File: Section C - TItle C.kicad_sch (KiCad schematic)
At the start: 1 part, among them U2 LT3042xMSE

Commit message: [Schématique test]
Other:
- moved on the sheet: U2
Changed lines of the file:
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@@
 	(symbol
 		(lib_id "Regulator_Linear:LT3042xMSE")
-		(at 203.2 68.58 0)
+		(at 228.6 72.39 0)
 		(unit 1)
 		(exclude_from_sim no)
@@
 		(fields_autoplaced yes)
 		(property "Reference" "U2"
-			(at 203.2 58.42 0)
+			(at 228.6 62.23 0)
 			(effects
 				(font
@@
 		)
 		(property "Value" "LT3042xMSE"
-			(at 203.2 60.96 0)
+			(at 228.6 64.77 0)
 			(effects
 				(font
@@
 		)
 		(property "Footprint" "Package_SO:MSOP-10-1EP_3x3mm_P0.5mm_EP2.2x3.1mm_Mask1.83x1.89mm_ThermalVias"
-			(at 203.2 60.325 0)
+			(at 228.6 64.135 0)
 			(effects
 				(font
@@
 		)
 		(property "Datasheet" "https://www.analog.com/media/en/technical-documentation/data-sheets/3042fb.pdf"
-			(at 203.2 68.58 0)
+			(at 228.6 72.39 0)
 			(effects
 				(font
@@
 		)
 		(property "Description" "200mA, Adjustable, Ultralow Noise, Ultrahigh PSRR RF Linear Regulator, MSOP-10"
-			(at 203.2 68.58 0)
+			(at 228.6 72.39 0)
 			(effects
 				(font

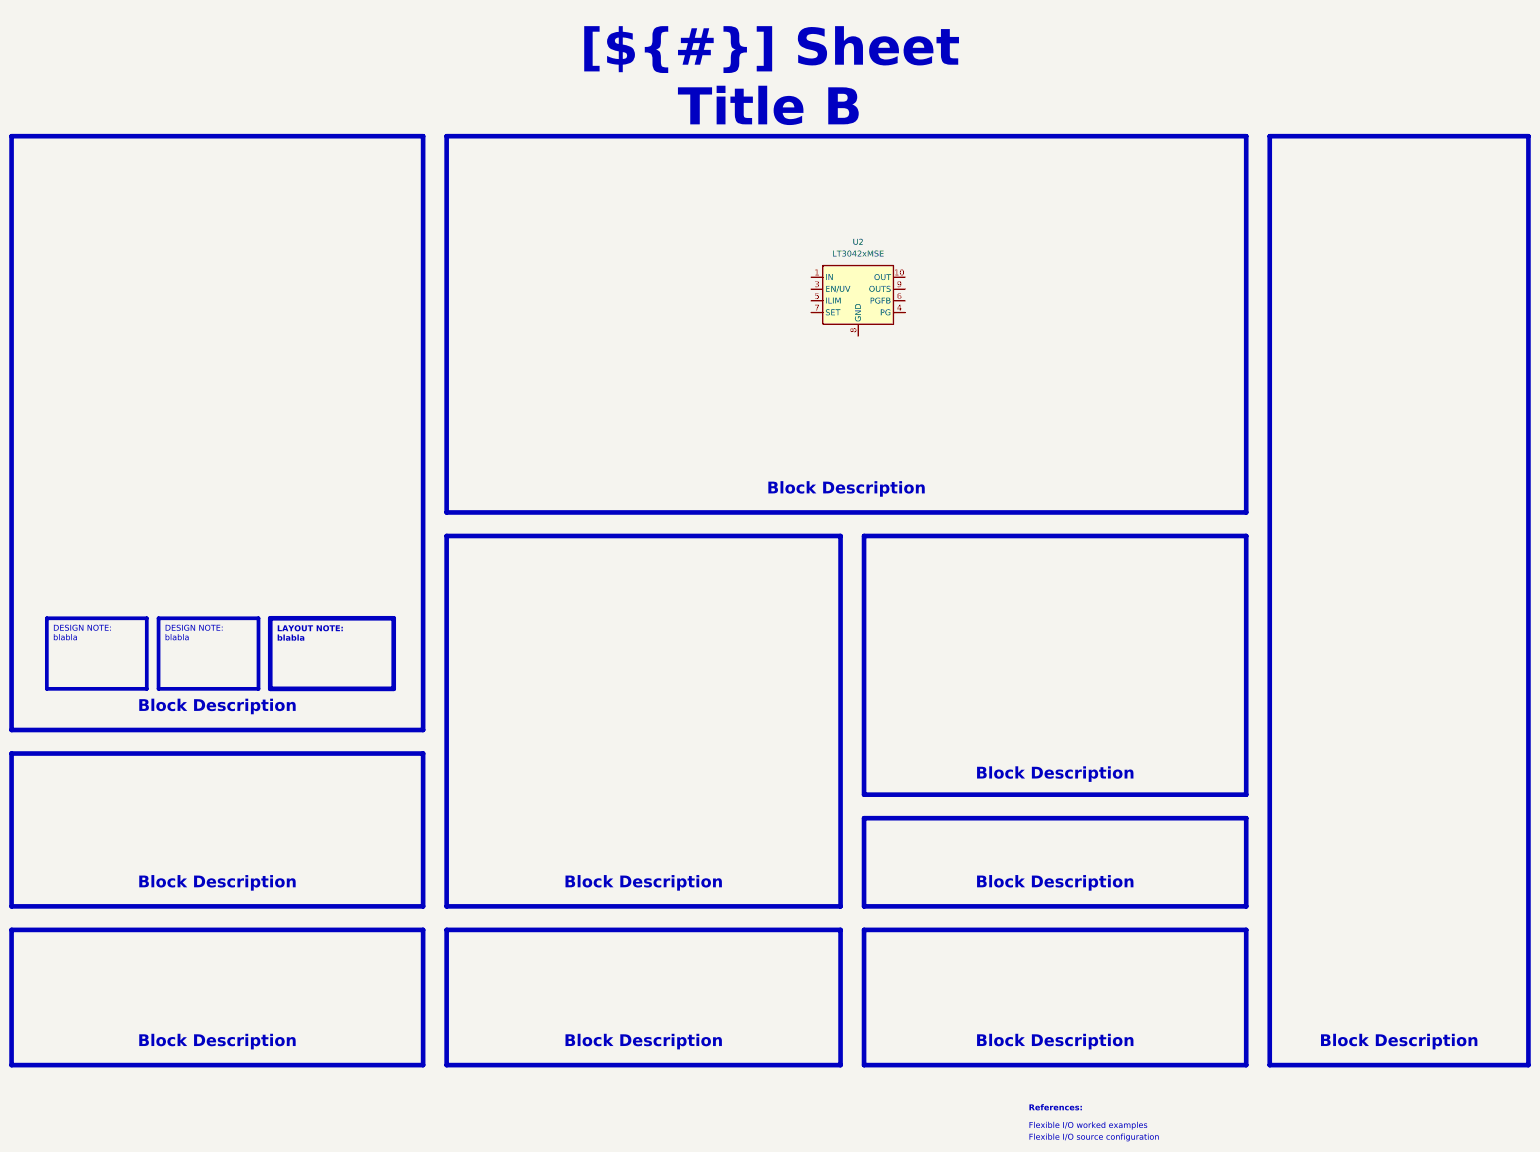
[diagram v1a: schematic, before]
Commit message: [FINISH LT3042 and ad TPS6108]
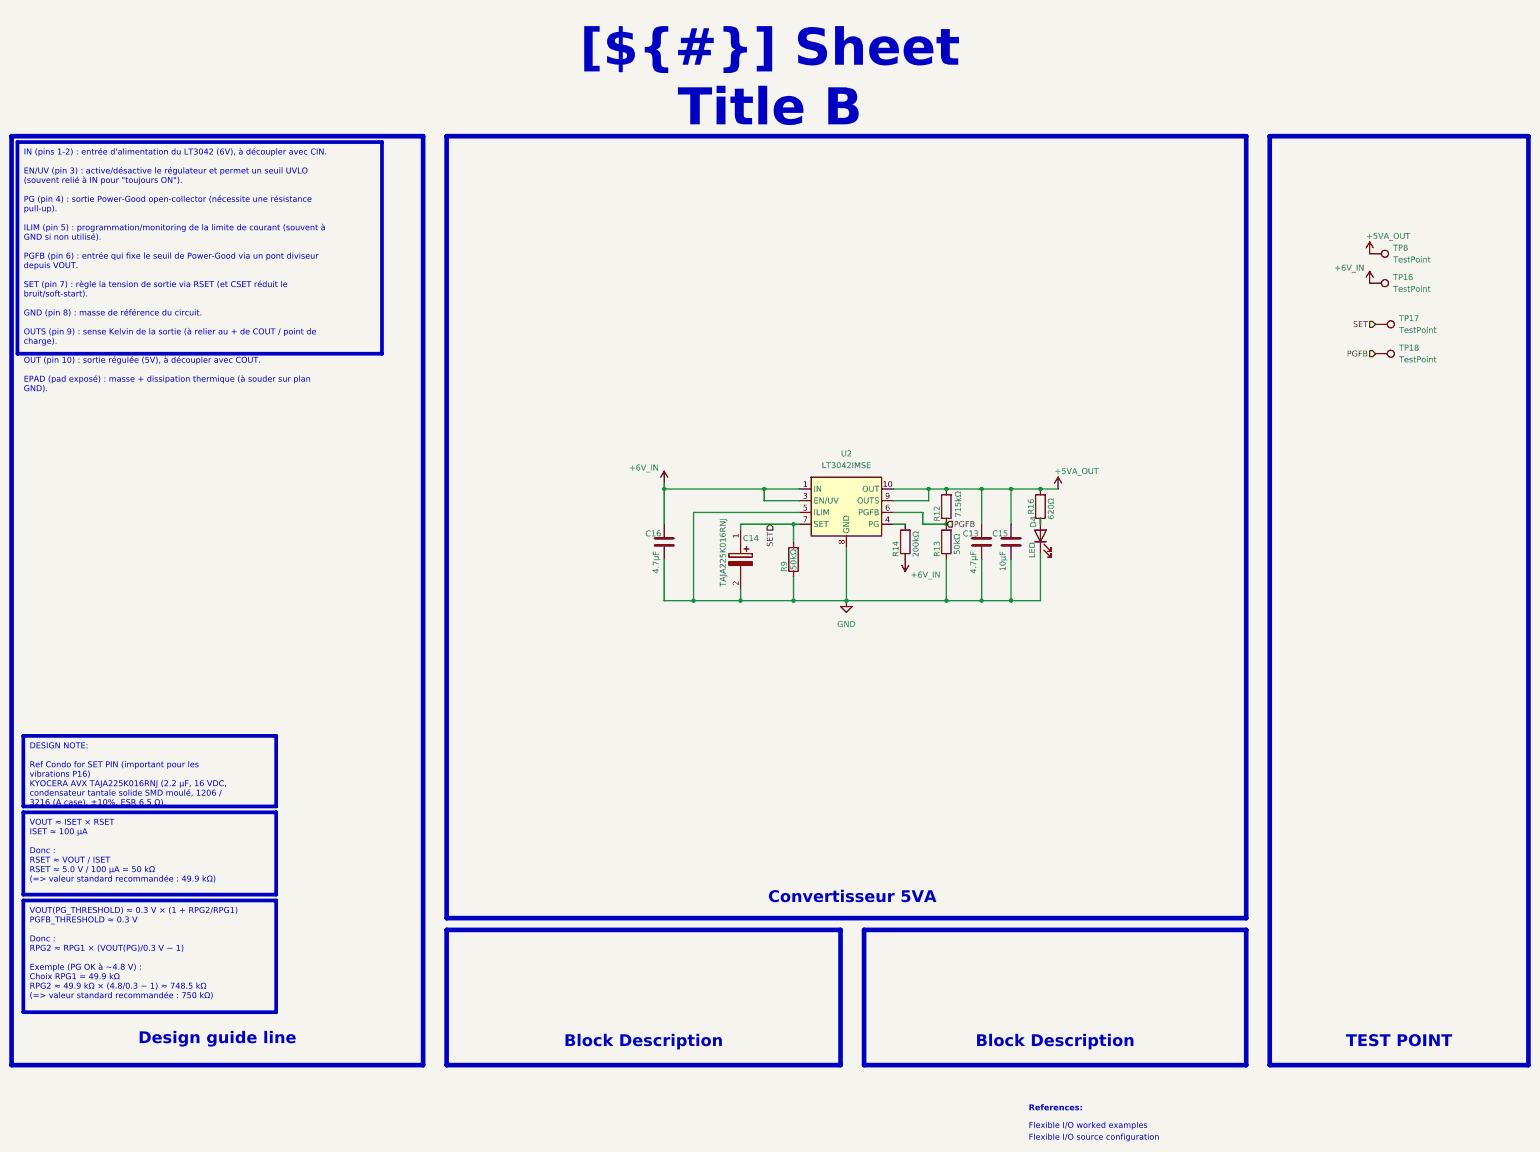
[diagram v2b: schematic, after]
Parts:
- added C13, C16: 4.7µF, Capacitor_SMD:C_0603_1608Metric, symbol Device:C
- added C14: TAJA225K016RNJ, CAPPM3216X180N, symbol TAJA225K016RNJ:TAJA225K016RNJ
- added C15: 10µF, Capacitor_SMD:C_0603_1608Metric, symbol Device:C
- added D4: LED, LED_SMD:LED_0603_1608Metric, symbol Device:LED
- added R12: 715kΩ, Resistor_SMD:R_0603_1608Metric, symbol Device:R
- added R13, R9: 50kΩ, Resistor_SMD:R_0603_1608Metric, symbol Device:R
- added R14: 200kΩ, Resistor_SMD:R_0603_1608Metric, symbol Device:R
- added R16: 620Ω, Resistor_SMD:R_0603_1608Metric, symbol Device:R
- added TP16, TP17, TP18, TP8: TestPoint, TestPoint:TestPoint_Pad_D2.0mm, symbol Connector:TestPoint
- U2: value LT3042xMSE -> LT3042IMSE
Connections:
- net +6V_IN: now reaches U2.1 (IN), U2.2 (IN)
- net +6V_IN: now also U2.3 (EN/UV), C16.1, R14.1, TP16.1
- net +5VA_OUT: now reaches U2.10 (OUT)
- net +5VA_OUT: now also U2.9 (OUTS), C13.1, C15.1, R12.2, R16.2, TP8.1
- net GND: now reaches U2.11 (GND), U2.8 (GND)
- net GND: now also U2.5 (ILIM), C13.2, C14.2 (-), C15.2, C16.2, D4.1 (K), R13.1, R9.1
- net at U2.4 (PG): now also R14.2
- net PGFB: now reaches U2.6 (PGFB)
- net PGFB: now also R12.1, R13.2, TP18.1
- net SET: now reaches U2.7 (SET)
- net SET: now also C14.1 (+), R9.2, TP17.1
- new net: D4.2 (A), R16.1
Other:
- moved on the sheet: U2

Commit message: [ADD TPS6108]
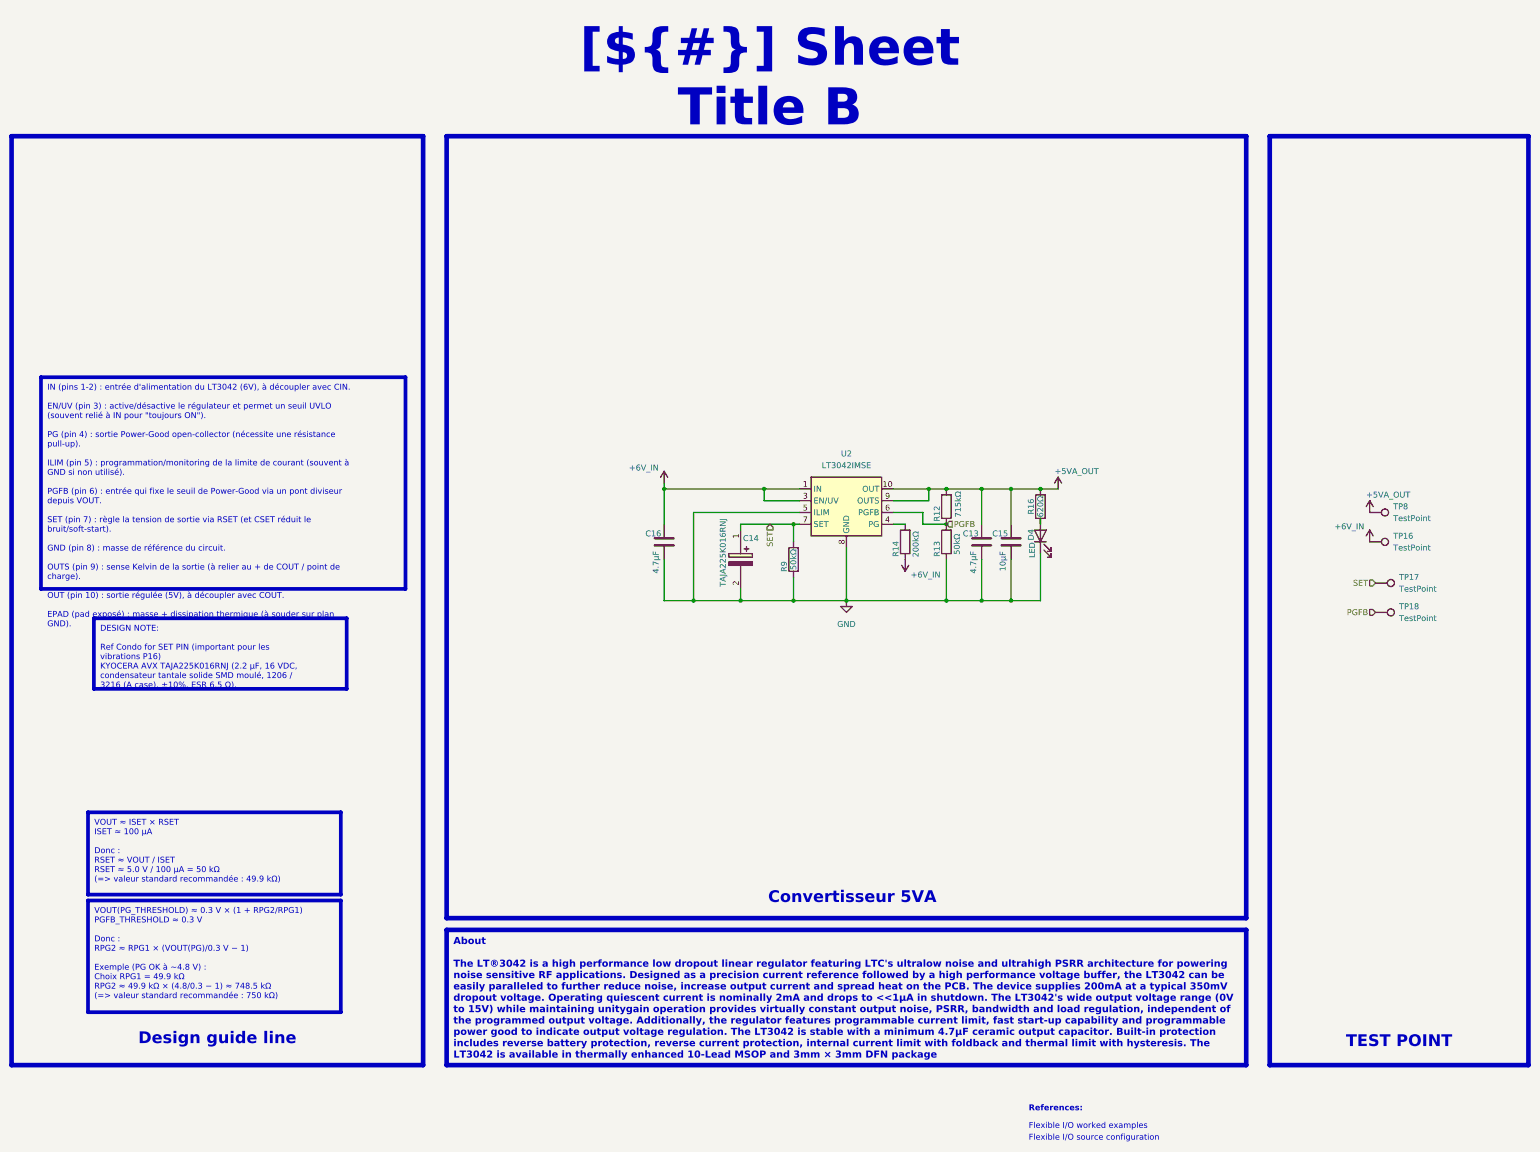
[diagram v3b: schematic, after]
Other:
- moved on the sheet: TP16, TP17, TP18, TP8

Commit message: [Finish schématique]
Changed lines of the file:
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@@
+	(wire
+		(pts
+			(xy 250.19 123.19) (xy 247.65 123.19)
+		)
+		(stroke
+			(width 0)
+			(type default)
+		)
+	)
 	(wire
 		(pts
@@
 	(wire
 		(pts
+			(xy 334.01 142.24) (xy 340.36 142.24)
+		)
+		(stroke
+			(width 0)
+			(type default)
+		)
+	)
+	(wire
+		(pts
 			(xy 243.84 118.11) (xy 243.84 115.57)
 		)
@@
 		(pts
 			(xy 226.06 128.27) (xy 226.06 139.7)
+		)
+		(stroke
+			(width 0)
+			(type default)
+		)
+	)
+	(wire
+		(pts
+			(xy 334.01 135.89) (xy 340.36 135.89)
 		)
 		(stroke
@@
 		)
 	)
-	(hierarchical_label "PGFB"
-		(shape input)
-		(at 247.65 123.19 0)
+	(label "SET"
+		(at 208.28 123.19 0)
 		(effects
 			(font
 				(size 1.27 1.27)
 			)
-			(justify left)
-		)
-	)
-	(hierarchical_label "SET"
-		(shape input)
-		(at 209.55 123.19 270)
+			(justify left bottom)
+		)
+	)
+	(label "SET"
+		(at 334.01 135.89 0)
 		(effects
 			(font
 				(size 1.27 1.27)
 			)
-			(justify right)
-		)
-	)
-	(hierarchical_label "SET"
-		(shape input)
-		(at 340.36 135.89 180)
+			(justify left bottom)
+		)
+	)
+	(label "PGFB"
+		(at 250.19 123.19 0)
 		(effects
 			(font
 				(size 1.27 1.27)
 			)
-			(justify right)
-		)
-	)
-	(hierarchical_label "PGFB"
-		(shape input)
-		(at 340.36 142.24 180)
+			(justify left bottom)
+		)
+	)
+	(label "PGFB"
+		(at 334.01 142.24 0)
 		(effects
 			(font
 				(size 1.27 1.27)
 			)
-			(justify right)
-		)
-	)
+			(justify left bottom)
+		)
+	)

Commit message: [Finish schématiq]
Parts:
- added TP23: TestPoint, TestPoint:TestPoint_Pad_D2.0mm, symbol Connector:TestPoint
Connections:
- net GND: now also TP23.1
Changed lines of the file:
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@@
 		)
 	)
-	(text_box "[${#}] ${TITLE}"
+	(text_box "[${#}] LT3042_6V_5VA"
 		(exclude_from_sim no)
 		(at 161.29 20.32 0)
-		(size 96.52 12.7)
+		(size 114.3 12.7)
 		(margins 5.9999 5.9999 5.9999 5.9999)
 		(stroke
 			(width -0.0001)
-			(type default)
+			(type solid)
 		)
 		(fill
@@
 	)
 	(symbol
+		(lib_id "power:GND")
+		(at 340.36 151.13 0)
+		(unit 1)
+		(exclude_from_sim no)
+		(in_bom yes)
+		(on_board yes)
+		(dnp no)
+		(fields_autoplaced yes)
+		(property "Reference" "#PWR037"
+			(at 340.36 157.48 0)
+			(effects
+				(font
+					(size 1.27 1.27)
+				)
+				(hide yes)
+			)
+		)
+		(property "Value" "GND"
+			(at 340.36 156.21 0)
+			(effects
+				(font
+					(size 1.27 1.27)
+				)
+			)
+		)
+		(property "Footprint" ""
+			(at 340.36 151.13 0)
+			(effects
+				(font
+					(size 1.27 1.27)
+				)
+				(hide yes)
+			)
+		)
+		(property "Datasheet" ""
+			(at 340.36 151.13 0)
+			(effects
+				(font
+					(size 1.27 1.27)
+				)
+				(hide yes)
+			)
+		)
+		(property "Description" "Power symbol creates a global label with name \"GND\" , ground"
+			(at 340.36 151.13 0)
+			(effects
+				(font
+					(size 1.27 1.27)
+				)
+				(hide yes)
+			)
+		)
+		(pin "1"
+		)
+		(instances
+			(project "Cellule_de_force_V2"
+				(path "/f9e05184-c88b-4a88-ae9c-ab2bdb32be7c/c5103ceb-5325-4a84-a025-9638a412984e/e744f3ce-03a6-44a6-8792-1447ef232b9a"
+					(reference "#PWR037")
+					(unit 1)
+				)
+			)
+		)
+	)
+	(symbol
 		(lib_id "power:+6V")
 		(at 339.09 127 0)
@@
 					(unit 1)
 				)
+			)
+		)
+	)
+	(symbol
+		(lib_id "Connector:TestPoint")
+		(at 340.36 151.13 270)
+		(unit 1)
+		(exclude_from_sim no)
+		(in_bom yes)
+		(on_board yes)
+		(dnp no)
+		(fields_autoplaced yes)
+		(property "Reference" "TP23"
+			(at 345.44 149.8599 90)
+			(effects
+				(font
+					(size 1.27 1.27)
+				)
+				(justify left)
+			)
+		)
+		(property "Value" "TestPoint"
+			(at 345.44 152.3999 90)
+			(effects
+				(font
+					(size 1.27 1.27)
+				)
+				(justify left)
+			)
+		)
+		(property "Footprint" "TestPoint:TestPoint_Pad_D2.0mm"
+			(at 340.36 156.21 0)
+			(effects
+				(font
+					(size 1.27 1.27)
+				)
+				(hide yes)
+			)
+		)
+		(property "Datasheet" "~"
+			(at 340.36 156.21 0)
+			(effects
+				(font
+					(size 1.27 1.27)
+				)
+				(hide yes)
+			)
+		)
+		(property "Description" "test point"
+			(at 340.36 151.13 0)
+			(effects
+				(font
+					(size 1.27 1.27)
+				)
+				(hide yes)
+			)
+		)
+		(pin "1"
+		)
+		(instances
+			(project "Cellule_de_force_V2"
+				(path "/f9e05184-c88b-4a88-ae9c-ab2bdb32be7c/c5103ceb-5325-4a84-a025-9638a412984e/e744f3ce-03a6-44a6-8792-1447ef232b9a"
+					(reference "TP23")
+					(unit 1)
+				)

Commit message: [PCB 4 layer]
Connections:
- net +5VA_OUT renamed +5VA
- net +6V_IN renamed +6V
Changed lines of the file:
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@@
 	(wire
 		(pts
+			(xy 335.28 151.13) (xy 340.36 151.13)
+		)
+		(stroke
+			(width 0)
+			(type default)
+		)
+	)
+	(wire
+		(pts
 			(xy 215.9 120.65) (xy 193.04 120.65)
 		)
@@
 		)
 		(property "Value" "715kΩ"
-			(at 250.19 118.872 90)
+			(at 247.65 119.38 90)
 			(effects
 				(font
-					(size 1.27 1.27)
+					(size 1.016 1.016)
 				)
 			)
@@
 	(symbol
 		(lib_id "power:GND")
-		(at 340.36 151.13 0)
+		(at 335.28 151.13 0)
 		(unit 1)
 		(exclude_from_sim no)
@@
 		(fields_autoplaced yes)
 		(property "Reference" "#PWR037"
-			(at 340.36 157.48 0)
+			(at 335.28 157.48 0)
 			(effects
 				(font
@@
 		)
 		(property "Value" "GND"
-			(at 340.36 156.21 0)
+			(at 335.28 156.21 0)
 			(effects
 				(font
@@
 		)
 		(property "Footprint" ""
-			(at 340.36 151.13 0)
+			(at 335.28 151.13 0)
 			(effects
 				(font
@@
 		)
 		(property "Datasheet" ""
-			(at 340.36 151.13 0)
+			(at 335.28 151.13 0)
 			(effects
 				(font
@@
 		)
 		(property "Description" "Power symbol creates a global label with name \"GND\" , ground"
-			(at 340.36 151.13 0)
+			(at 335.28 151.13 0)
 			(effects
 				(font
@@
 	(symbol
 		(lib_id "power:+6V")
-		(at 339.09 127 0)
+		(at 339.09 127 90)
 		(unit 1)
 		(exclude_from_sim no)
@@
 		(dnp no)
 		(property "Reference" "#PWR021"
-			(at 339.09 130.81 0)
+			(at 342.9 127 0)
 			(effects
 				(font
@@
 			)
 		)
-		(property "Value" "+6V_IN"
-			(at 331.47 123.698 0)
+		(property "Value" "+6V"
+			(at 337.312 125.476 90)
 			(effects
 				(font
@@
 	(symbol
 		(lib_id "power:+5VA")
-		(at 339.09 120.65 0)
+		(at 339.09 120.65 90)
 		(unit 1)
 		(exclude_from_sim no)
@@
 		(dnp no)
 		(property "Reference" "#PWR017"
-			(at 339.09 124.46 0)
+			(at 342.9 120.65 0)
 			(effects
 				(font
@@
 			)
 		)
-		(property "Value" "+5VA_OUT"
-			(at 338.328 116.84 0)
+		(property "Value" "+5VA"
+			(at 339.09 119.126 90)
 			(effects
 				(font
@@
 		)
 		(property "Value" "200kΩ"
-			(at 241.046 127.508 90)
+			(at 238.76 127.254 90)
 			(effects
 				(font
-					(size 1.27 1.27)
+					(size 1.016 1.016)
 				)
 			)
@@
 			(effects
 				(font
-					(size 1.27 1.27)
+					(size 1.016 1.016)
 				)
 			)
@@
 			)
 		)
-		(property "Value" "+6V_IN"
+		(property "Value" "+6V"
 			(at 179.07 110.998 0)
 			(effects
@@
 			)
 		)
-		(property "Value" "+5VA_OUT"
+		(property "Value" "+5VA"
 			(at 271.018 111.76 0)
 			(effects
@@
 			(effects
 				(font
-					(size 1.27 1.27)
+					(size 1.016 1.016)
 				)
 			)
@@
 			)
 		)
-		(property "Value" "+6V_IN"
-			(at 246.38 134.112 0)
+		(property "Value" "+6V"
+			(at 236.728 134.62 0)
 			(effects
 				(font
@@
 		)
 		(property "Value" "50kΩ"
-			(at 249.936 127.508 90)
+			(at 247.65 127 90)
 			(effects
 				(font
-					(size 1.27 1.27)
+					(size 1.016 1.016)
 				)
 			)

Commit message: [PCB V1]
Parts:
- removed TP16, TP18, TP23, TP8: TestPoint, TestPoint:TestPoint_Pad_D2.0mm, symbol Connector:TestPoint
- added TP10, TP11, TP12, TP13: TestPoint, TestPoint:TestPoint_Pad_D1.5mm, symbol Connector:TestPoint
- TP17: footprint TestPoint:TestPoint_Pad_D2.0mm -> TestPoint:TestPoint_Pad_D1.5mm
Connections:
- net +5VA: now also TP10.1
- net +6V: now also TP11.1
- net PGFB: now also TP13.1
- net SET: now also TP12.1; no longer TP17.1
- net PG: now reaches R14.2, U2.4 (PG)
- net PG: now also TP17.1
